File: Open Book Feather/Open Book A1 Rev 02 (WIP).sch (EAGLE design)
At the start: 127 parts, among them J1 SJ-43514-SMT, J2 10118193-0001LF, Q1 DMG341, Q2 IRLML0100, SW1 SPDT_SWITCH, U1 AP2112-3.3, U2 MCP73831T-2ACI/OT, U3 ATSAMD51J64-TQFP(10X10), U4 GD25Q16C (or GD25Q32C), U5 74AC165D, U6 GD25Q16C (or GD25Q32C), U7 23K256-I/SN, U8 MAX4466EXK+T, X1 JSTPH, X2 2x5 0.05" SWD

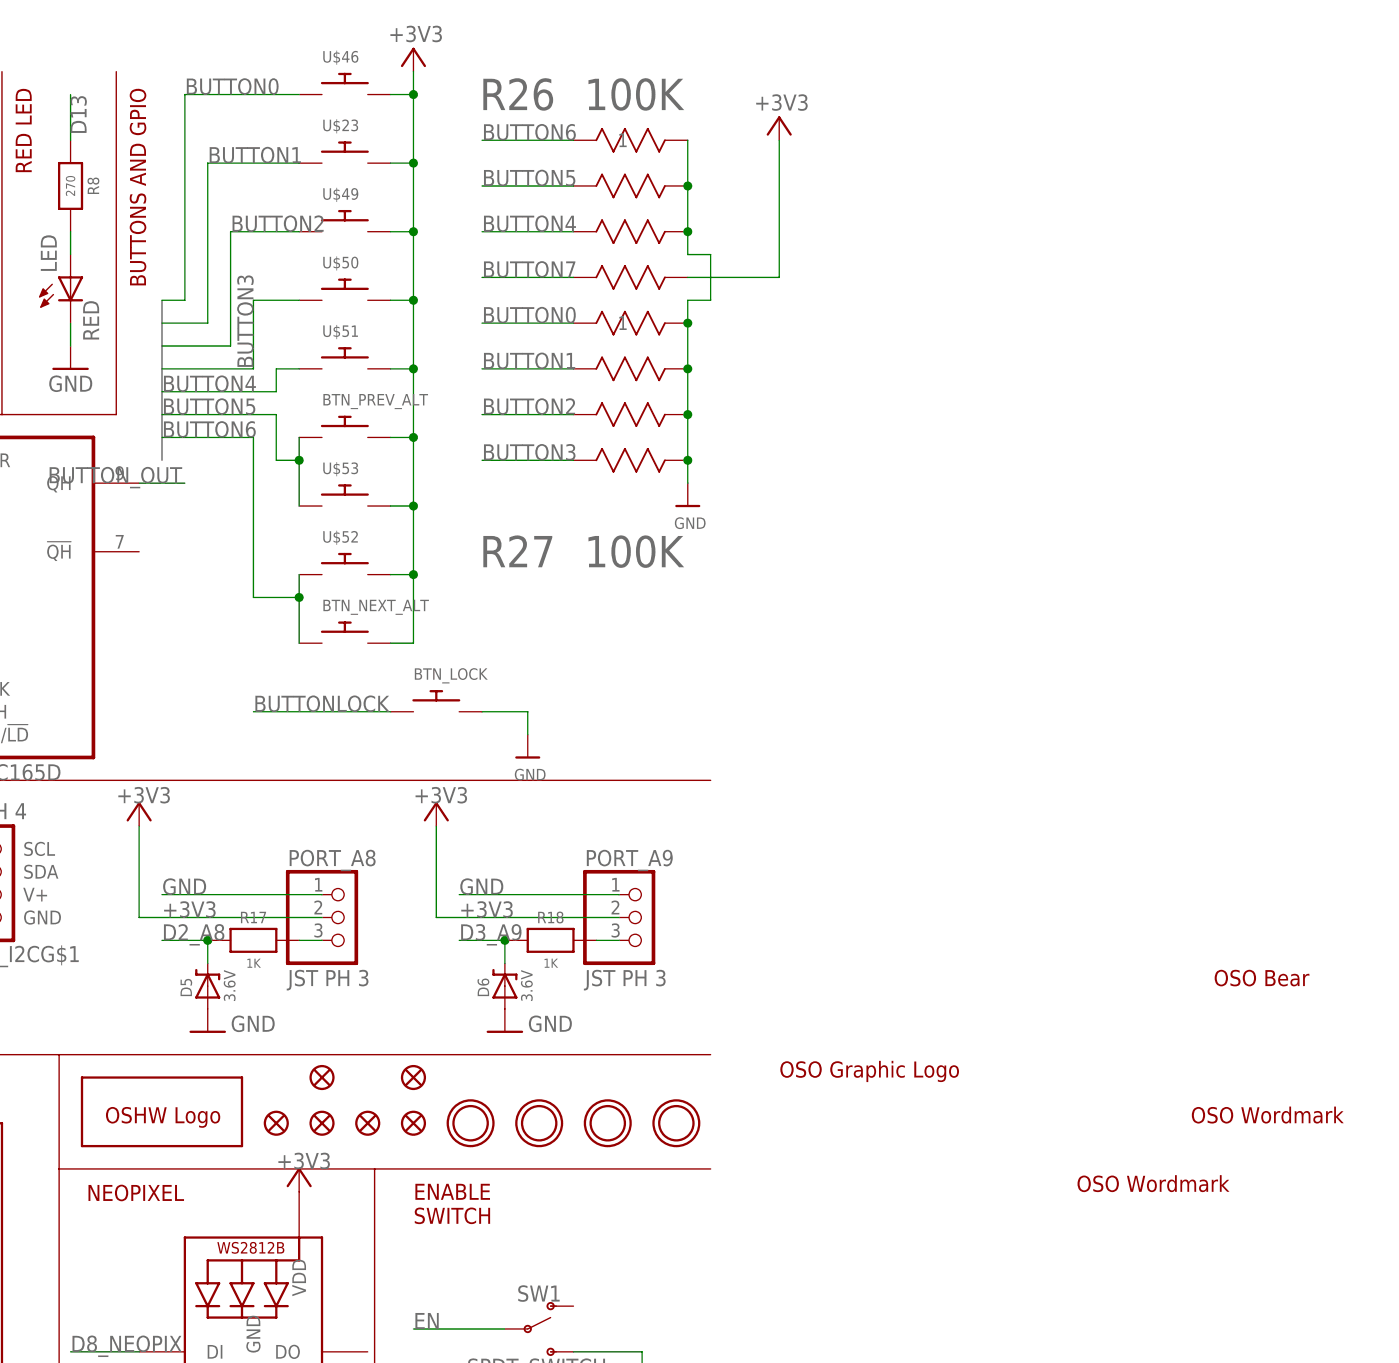
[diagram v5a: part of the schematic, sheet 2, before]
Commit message: move leds to bottom, improve placement
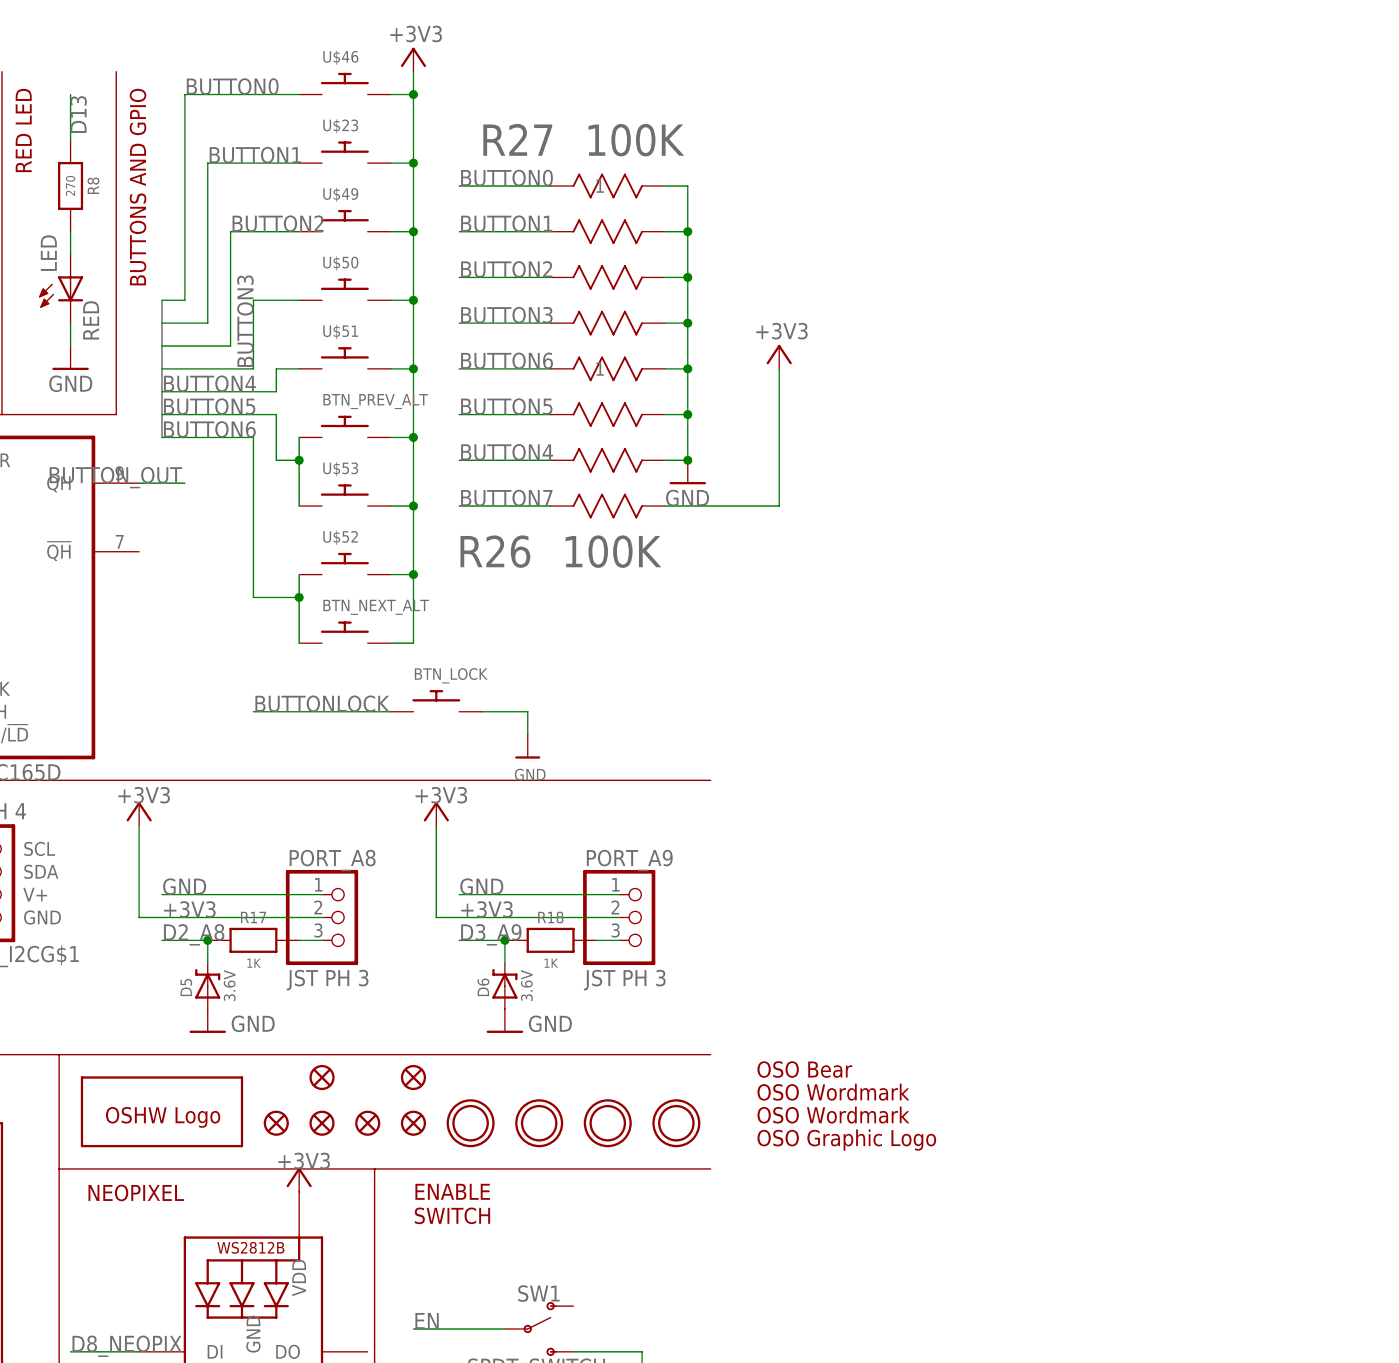
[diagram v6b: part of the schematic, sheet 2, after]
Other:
- note added: "BUTTON7 is the SD Card Detect signal, so it needs a pull-up rather than a pulldown."
- note removed: "This looks ridic but BUTTON7 is now the SD Card Detect line, and it needs a pull-up rather than a pulldown."
- moved on the sheet: R26, R27

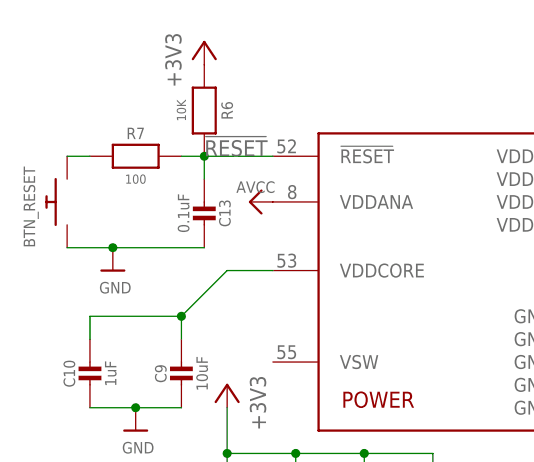
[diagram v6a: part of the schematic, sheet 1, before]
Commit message: improved silkscreen documentation
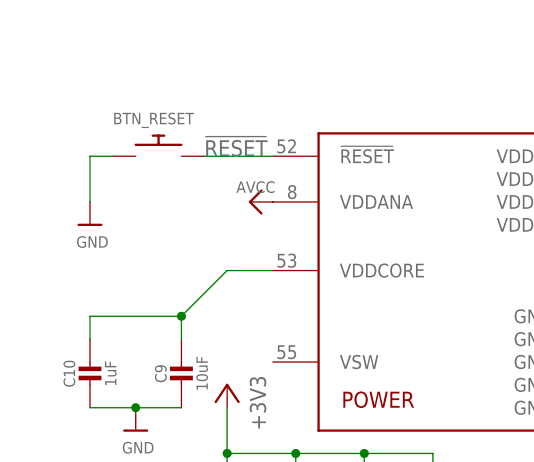
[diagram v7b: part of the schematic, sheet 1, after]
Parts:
- removed C13: 0.1uF, microbuilder:CAP_CERAMIC0805_10MGAP
- removed R6: 10K, microbuilder:RESISTOR0805_10MGAP
- removed R7: 100, microbuilder:RESISTOR0805_10MGAP
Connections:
- removed net N$1: BTN_RESET.P$2, R7.1
- net !RESET: now also BTN_RESET.P$2; no longer C13.2, R6.2, R7.2
- net +3V3: no longer R6.1
- net GND: no longer C13.1
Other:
- moved on the sheet: BTN_RESET
